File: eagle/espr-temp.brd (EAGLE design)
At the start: 66.3 x 31.8 mm, 34 parts, among them IC1 FT231XS-R, IC2 ESP-WROOM-02, IC3 AM2320

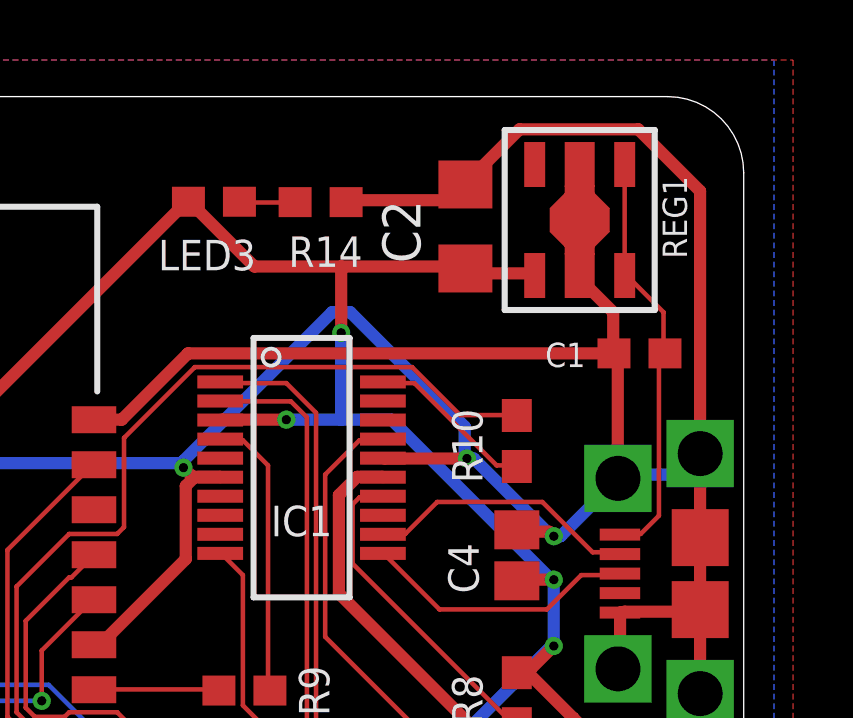
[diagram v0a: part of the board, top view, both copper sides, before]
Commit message: fix some ERC errors
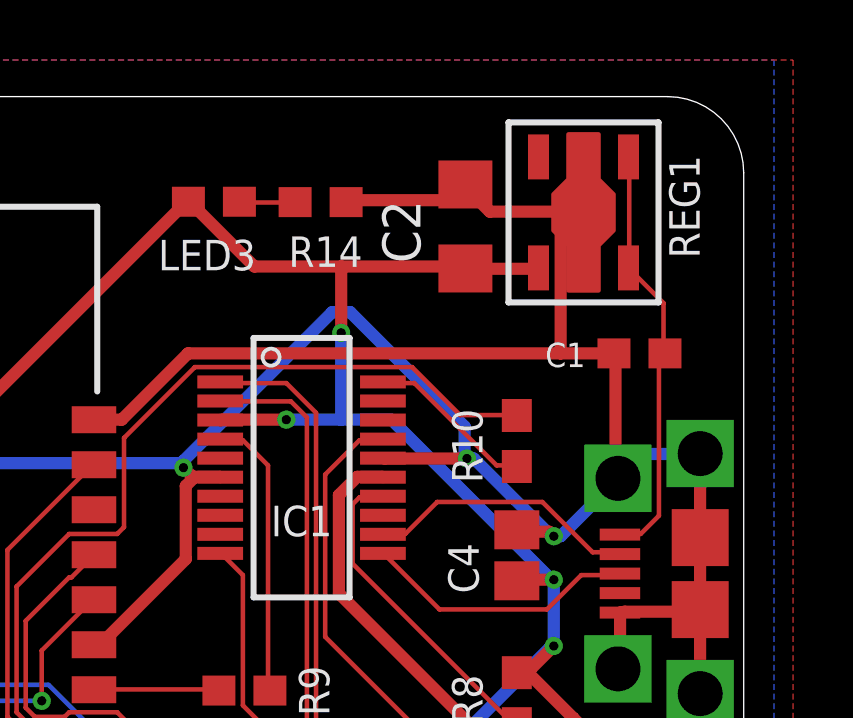
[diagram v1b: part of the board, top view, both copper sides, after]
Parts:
- REG1: value NJM2884U1 -> NJM2884; device regulator:SOT-89-5 -> regulator:NJM2884-SOT-89-5
- moved REG1 0.28 mm to (61.0, 27.9)
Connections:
- net GND: now also REG1.2; no longer REG1.2_1
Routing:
- net GND: track 182.7 -> 171.1 mm

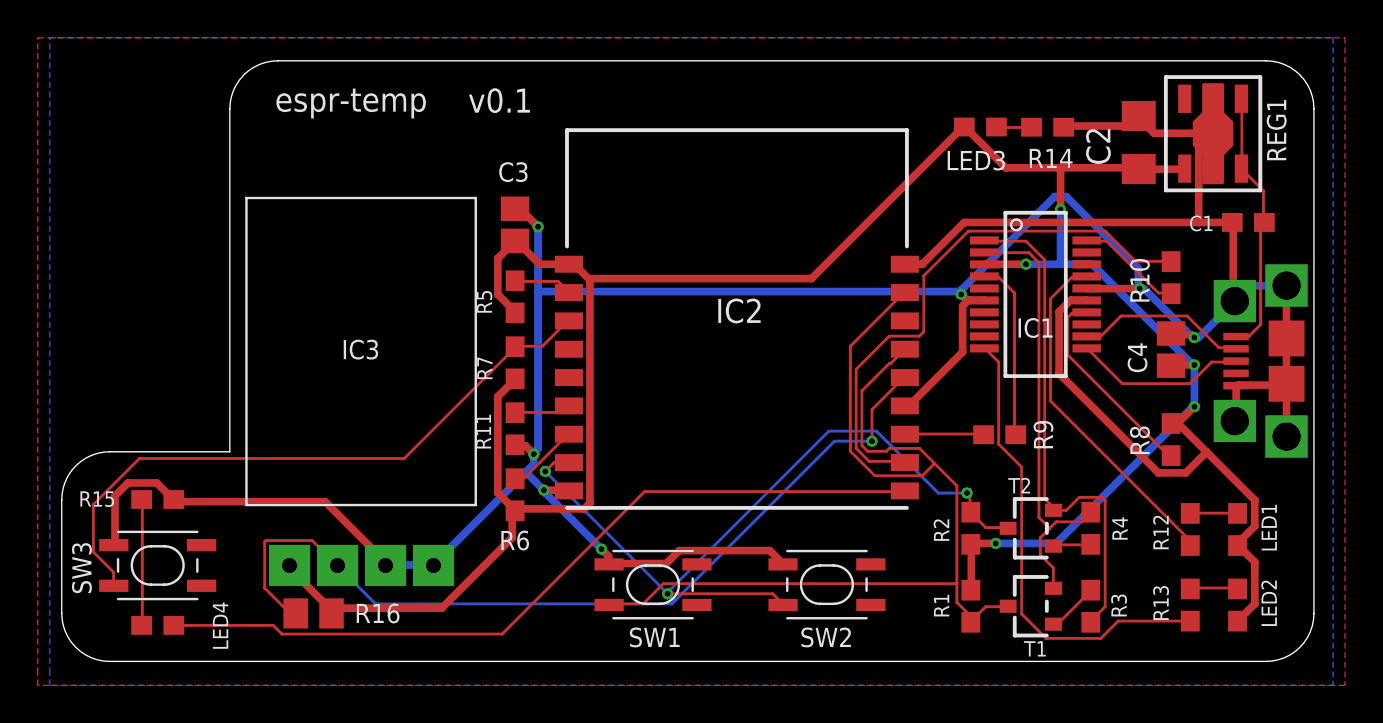
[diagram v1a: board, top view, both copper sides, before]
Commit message: change to GND from tRistrict for WROOM2 library
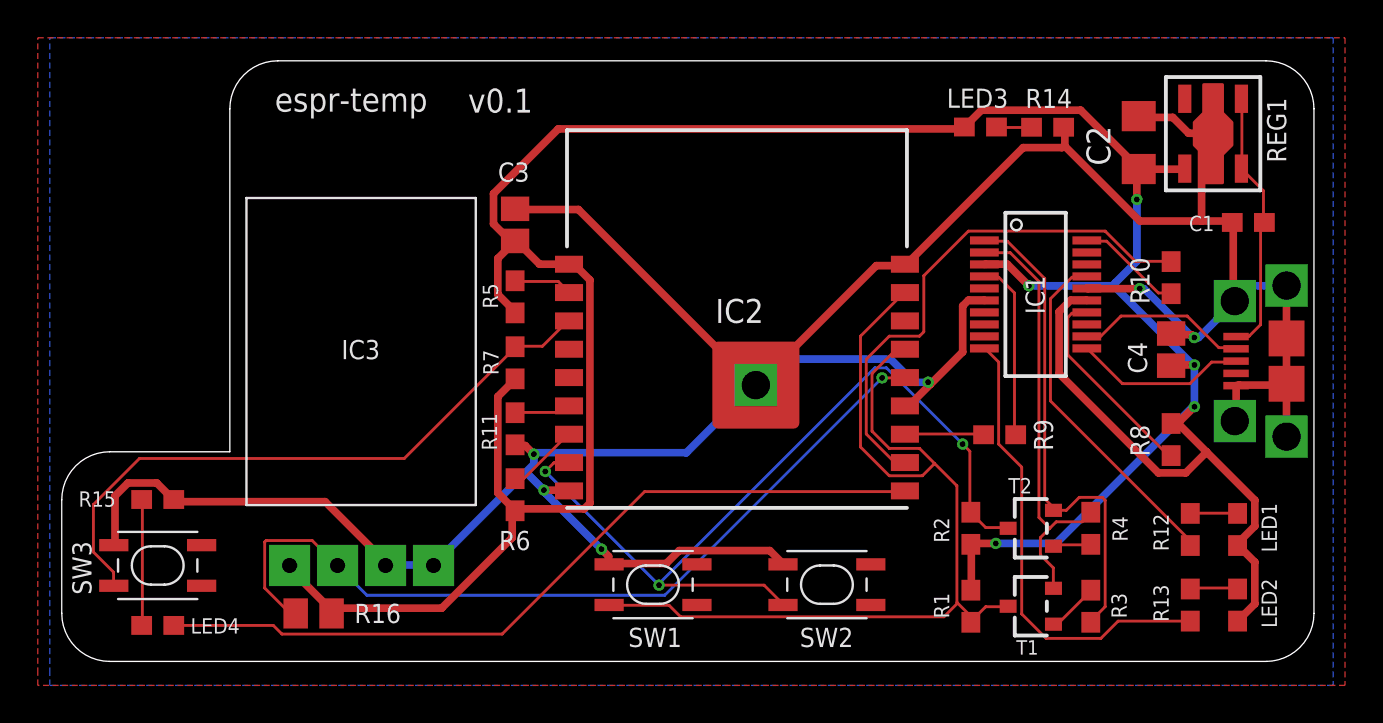
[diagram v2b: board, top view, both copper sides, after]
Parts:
- IC2: device esp-wroom-02:FRONT-FACE -> esp-wroom-02:ESP-WROOM-02
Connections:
- net GND: now also IC2.19
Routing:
- net +3V3: track 154.9 -> 163.6 mm
- net IO0: track 41.2 -> 45.7 mm
- net RESET: track 55.8 -> 54.0 mm
- net IO5: track 45.9 -> 44.5 mm
- net N$11: track 29.2 -> 28.0 mm
- net DTR: track 27.0 -> 26.4 mm
- net RTS: track 23.6 -> 23.0 mm
- net GND: track 171.1 -> 170.7 mm, vias 7 -> 6
